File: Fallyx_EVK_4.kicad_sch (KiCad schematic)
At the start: 0 parts

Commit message: continued design work
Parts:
- added C10, C17, C18, C24, C25: 10pF, Capacitor_SMD:C_0402_1005Metric, symbol Device:C
- added C11, C13, C23: 1uF, Capacitor_SMD:C_0402_1005Metric, symbol Device:C
- added C12, C15, C16, C19, C20, C21, C22, C26: 0.1uF, Capacitor_SMD:C_0402_1005Metric, symbol Device:C
- added C14: 4.7uF, Capacitor_SMD:C_0603_1608Metric, symbol Device:C
- added C9: 22nuF, Capacitor_SMD:C_0402_1005Metric, symbol Device:C
- added FB1: 600R/0.7A, symbol Device:FerriteBead
- added R11, R14: 10k, Resistor_SMD:R_0402_1005Metric, symbol Device:R_US
- added R12: 1k, Resistor_SMD:R_0402_1005Metric, symbol Device:R_US
- added R13: 0R, Resistor_SMD:R_0805_2012Metric, symbol Device:R_US
- added U4: STM32L431VCIx, Package_BGA:UFBGA-100_7x7mm_Layout12x12_P0.5mm, symbol MCU_ST_STM32L4:STM32L431VCIx
- added U5: MX25R3235FZNxx0, Package_SON:WSON-8-1EP_6x5mm_P1.27mm_EP3.4x4mm, symbol Memory_Flash:MX25R3235FZNxx0
- added X1: 8MHz, ECS-320-CDX-2094:XTAL_ECS-320-CDX-2094, symbol Device:Crystal
- added X2: 32.768kHz, CM9V-T1A-32.768KHZ-7PF-100PPM-TA-QC:XTAL_CM9V-T1A-32.768KHZ-7PF-100PPM-TA-QC, symbol Device:Crystal
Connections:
- new net: C10.1, R12.2, U4.H2 (NRST)
- new net 1V8: C14.1, C15.1, C16.1, C19.1, C20.1, C21.1, C22.1, FB1.2, R14.2, U4.C11 (VDD), U4.C4 (VDD), U4.G11 (VDD), U4.G12 (VDD), U4.G2 (VDD), U4.H3 (VDD), U5.8 (VCC)
- new net BLE_UART_RX: U4.A6 (PD5)
- new net BLE_UART_TX: U4.B6 (PD6)
- new net ENHV: U4.D12 (PC9)
- new net ENLV: U4.B11 (PC10)
- new net GND: C10.2, C11.2, C12.2, C13.2, C14.2, C15.2, C16.2, C17.2, C18.2, C19.2, C20.2, C21.2, C22.2, C23.2, C24.2, C25.2, C26.2, C9.2, R11.1, U4.D3 (VSS), U4.E3 (VSS), U4.F11 (VSS), U4.F12 (VSS), U4.F2 (VSS), U4.J1 (VSSA), U4.K1 (VREF-), U5.4 (GND), U5.9 (GND)
- new net GPOUT: U4.J3 (PC2)
- new net I2C1_SCL: U4.A3 (PB8)
- new net I2C1_SDA: U4.B3 (PB9)
- new net I2C2_SCL: U4.L10 (PB10)
- new net I2C2_SDA: U4.L11 (PB11)
- new net JTMS_SWCLK: U4.A10 (PA14)
- new net JTMS_SWDIO: U4.A11 (PA13)
- new net MCP_STAT: U4.B7 (PD4)
- new net NRF_nRESET: U4.B1 (PE4)
- new net PA0: U4.L2 (PA0)
- new net PA1: U4.M2 (PA1)
- new net PA10: U4.C12 (PA10)
- new net PA9: U4.D10 (PA9)
- new net PB0: U4.M5 (PB0)
- new net PB1: U4.M6 (PB1)
- new net PB12: U4.L12 (PB12)
- new net PB13: U4.K12 (PB13)
- new net PC0: U4.H1 (PC0)
- new net PC1: U4.J2 (PC1)
- new net PC4: U4.K5 (PC4)
- new net PC5: U4.L5 (PC5)
- new net PC6: U4.E12 (PC6)
- new net PD7: U4.A5 (PD7)
- new net PE3: U4.A1 (PE3)
- new net PE6: U4.D2 (PE6)
- new net PE7: U4.M7 (PE7)
- new net PE9: U4.M8 (PE9)
- new net QSPI_BK1_CLK: U4.L8 (PE10), U5.6 (SCLK)
- new net QSPI_BK1_IO0: U4.L9 (PE12), U5.5 (SI/SIO0)
- new net QSPI_BK1_IO1: U4.M10 (PE13), U5.2 (SO/SIO1)
- new net QSPI_BK1_IO2: U4.M11 (PE14), U5.3 (~{WP}/SIO2)
- new net QSPI_BK1_IO3: U4.M12 (PE15), U5.7 (~{RESET}/SIO3)
- new net QSPI_BK1_NCS: R14.1, U4.M9 (PE11), U5.1 (~{CS})
- new net SINK1: U4.K8 (PD9)
- new net SPI1_MISO: U4.L4 (PA6)
- new net SPI1_MOSI: U4.M4 (PA7)
- new net SPI1_SCK: U4.K4 (PA5)
- new net SPI_LEVEL_EN: U4.B8 (PD3)
- new net STM_BOOT0: R11.2, U4.A4 (PH3)
- new net STM_HS_N: C17.1, U4.F1 (PH0), X1.2
- new net STM_HS_P: C18.1, U4.G1 (PH1), X1.1
- new net STM_RTC_N: C24.1, U4.D1 (PC14), X2.2
- new net STM_RTC_P: C25.1, U4.E1 (PC15), X2.1
- new net STM_STATUS0: U4.K9 (PD8)
- new net STM_STATUS1: U4.J11 (PD11)
- new net STM_STATUS2: U4.J12 (PD10)
- new net STM_VDDA: C12.1, C13.1, C23.1, C26.1, FB1.1, U4.L1 (VREF+), U4.M1 (VDDA)
- new net STM_nRST: C9.1, R12.1
- new net VBAT: C11.1, R13.2, U4.E2 (VBAT)
- new net VRTC: R13.1
- no-connect marks 0 -> 32
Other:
- note added: "HIGH FREQ CLK"
- note added: "LOW FREQ CLK"
- note added: "MX25R6435FZNIL0"
- note added: "SPI FLASH"
- note added: "STM32 CONTROLLER"

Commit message: review edits
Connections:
- net PC13: now reaches U4.C1 (PC13)
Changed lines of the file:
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@@
+		)
+	)
+	(global_label "PC13"
+		(shape input)
+		(at 133.35 162.56 0)
+		(fields_autoplaced yes)
+		(effects
+			(font
+				(size 1.27 1.27)
+				(color 0 60 135 1)
+			)
+			(justify left)
+		)
+		(property "Intersheetrefs" "${INTERSHEET_REFS}"
+			(at 141.2942 162.56 0)
+			(effects
+				(font
+					(size 1.27 1.27)
+				)
+				(justify left)
+				(hide yes)
+			)
 		)
 	)

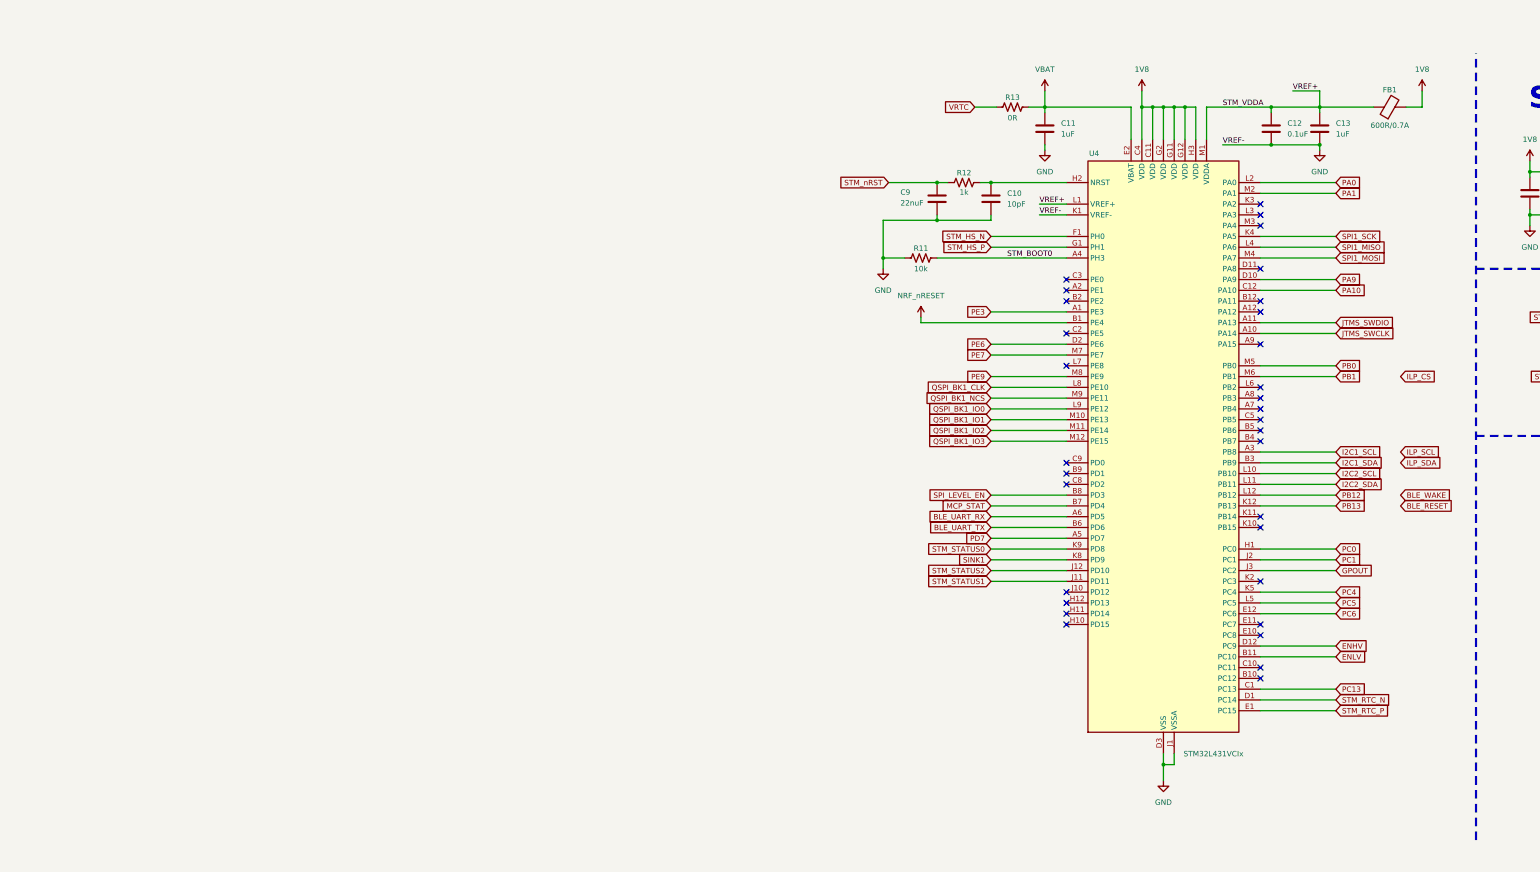
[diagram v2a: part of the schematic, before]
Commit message: Updated for new BLE modules
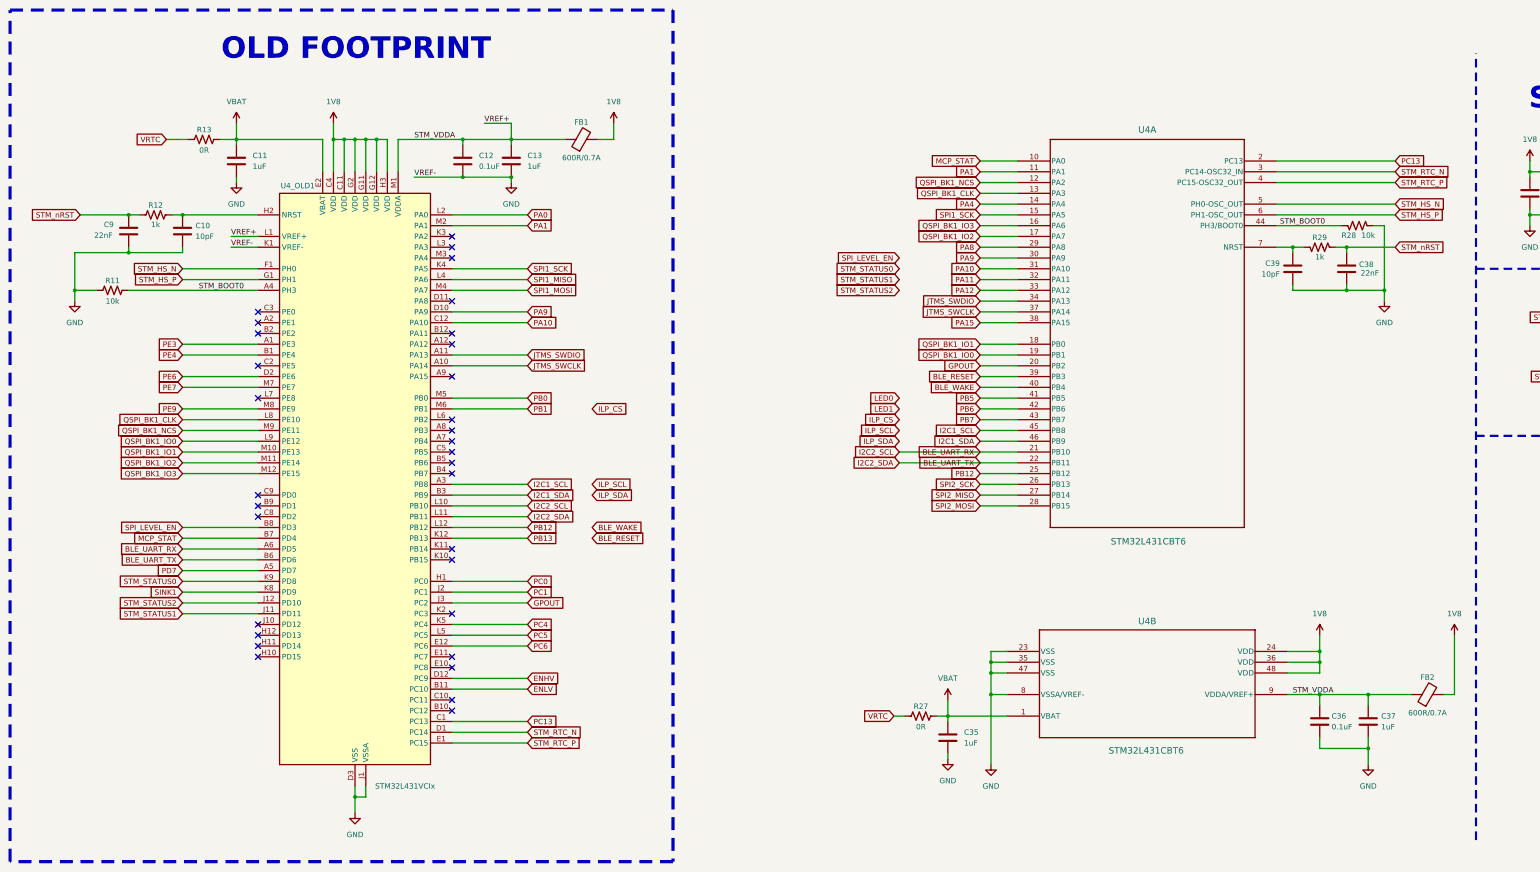
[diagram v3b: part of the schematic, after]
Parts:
- added C35, C37: 1uF, Capacitor_SMD:C_0402_1005Metric, symbol Device:C
- added C36: 0.1uF, Capacitor_SMD:C_0402_1005Metric, symbol Device:C
- added C38: 22nF, Capacitor_SMD:C_0402_1005Metric, symbol Device:C
- added C39: 10pF, Capacitor_SMD:C_0402_1005Metric, symbol Device:C
- added FB2: 600R/0.7A, Resistor_SMD:R_0402_1005Metric, symbol Device:FerriteBead
- added R27: 0R, Resistor_SMD:R_0805_2012Metric, symbol Device:R_US
- added R28: 10k, Resistor_SMD:R_0402_1005Metric, symbol Device:R_US
- added R29: 1k, Resistor_SMD:R_0402_1005Metric, symbol Device:R_US
- added U4: STM32L431CBT6, STM32L431CBT6:LQFP-48, symbol STM32L431CBT6:STM32L431CBT6
- C9: value 22nuF -> 22nF
- renumbered U4 to U4_OLD1
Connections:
- net I2C2_SCL is gone; now on net BLE_UART_RX: U4_OLD1.L10 (PB10)
- net I2C2_SDA is gone; now on net BLE_UART_TX: U4_OLD1.L11 (PB11)
- net 1V8: now also FB2.2, U4.24 (VDD), U4.36 (VDD), U4.48 (VDD)
- net BLE_RESET: now also U4.39 (PB3)
- net BLE_UART_RX: now also U4.21 (PB10)
- net BLE_UART_TX: now also U4.22 (PB11)
- net BLE_WAKE: now also U4.40 (PB4)
- net GND: now also C35.2, C36.2, C37.2, C38.2, C39.2, R28.1, U4.23 (VSS), U4.35 (VSS), U4.47 (VSS), U4.8 (VSSA/VREF-)
- net GPOUT: now also U4.20 (PB2)
- net I2C1_SCL: now also U4.45 (PB8)
- net I2C1_SDA: now also U4.46 (PB9)
- net JTMS_SWCLK: now also U4.37 (PA14)
- net JTMS_SWDIO: now also U4.34 (PA13)
- net MCP_STAT: now also U4.10 (PA0)
- net PA1: now also U4.11 (PA1)
- net PA10: now also U4.31 (PA10)
- net PA9: now also U4.30 (PA9)
- net PB12: now also U4.25 (PB12)
- net PC13: now also U4.2 (PC13)
- net QSPI_BK1_CLK: now also U4.13 (PA3)
- net QSPI_BK1_IO0: now also U4.19 (PB1)
- net QSPI_BK1_IO1: now also U4.18 (PB0)
- net QSPI_BK1_IO2: now also U4.17 (PA7)
- net QSPI_BK1_IO3: now also U4.16 (PA6)
- net QSPI_BK1_NCS: now also U4.12 (PA2)
- net SPI1_SCK: now also U4.15 (PA5)
- net STM_BOOT0: now also R28.2, U4.44 (PH3/BOOT0)
- net STM_HS_N: now also U4.5 (PH0-OSC_OUT)
- net STM_HS_P: now also U4.6 (PH1-OSC_OUT)
- net STM_RTC_N: now also U4.3 (PC14-OSC32_IN)
- net STM_RTC_P: now also U4.4 (PC15-OSC32_OUT)
- net STM_VDDA: now also C36.1, C37.1, FB2.1, U4.9 (VDDA/VREF+)
- net STM_nRST: now also C38.1, R29.1
- net VBAT: now also C35.1, R27.2, U4.1 (VBAT)
- net VRTC: now also R27.1
- net NRF_nRESET renamed PE4
- new net: C39.1, R29.2, U4.7 (NRST)
- new net PA11: U4.32 (PA11)
- new net PA12: U4.33 (PA12)
- new net PA15: U4.38 (PA15)
- new net PA4: U4.14 (PA4)
- new net PA8: U4.29 (PA8)
- new net PB5: U4.41 (PB5)
- new net PB6: U4.42 (PB6)
- new net PB7: U4.43 (PB7)
- new net SPI2_MISO: U4.27 (PB14)
- new net SPI2_MOSI: U4.28 (PB15)
- new net SPI2_SCK: U4.26 (PB13)
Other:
- note added: "OLD FOOTPRINT"
- moved on the sheet: C10, C11, C12, C13, C9, FB1, R11, R12, R13, U4_OLD1
